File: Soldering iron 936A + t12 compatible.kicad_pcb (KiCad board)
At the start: 2 copper layers, 97 x 67 mm, 112 parts, among them J1 DC INPUT, J2 USB TO SERIAL, J3 AC input, J4 output_connector, J5 mosfet_driver_future_backup, J6 OLED, J7 USB C BREAKOUT BOARD, Q1 IRF9540N, Q2 BC547, SW1 RotaryEncoder_Switch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

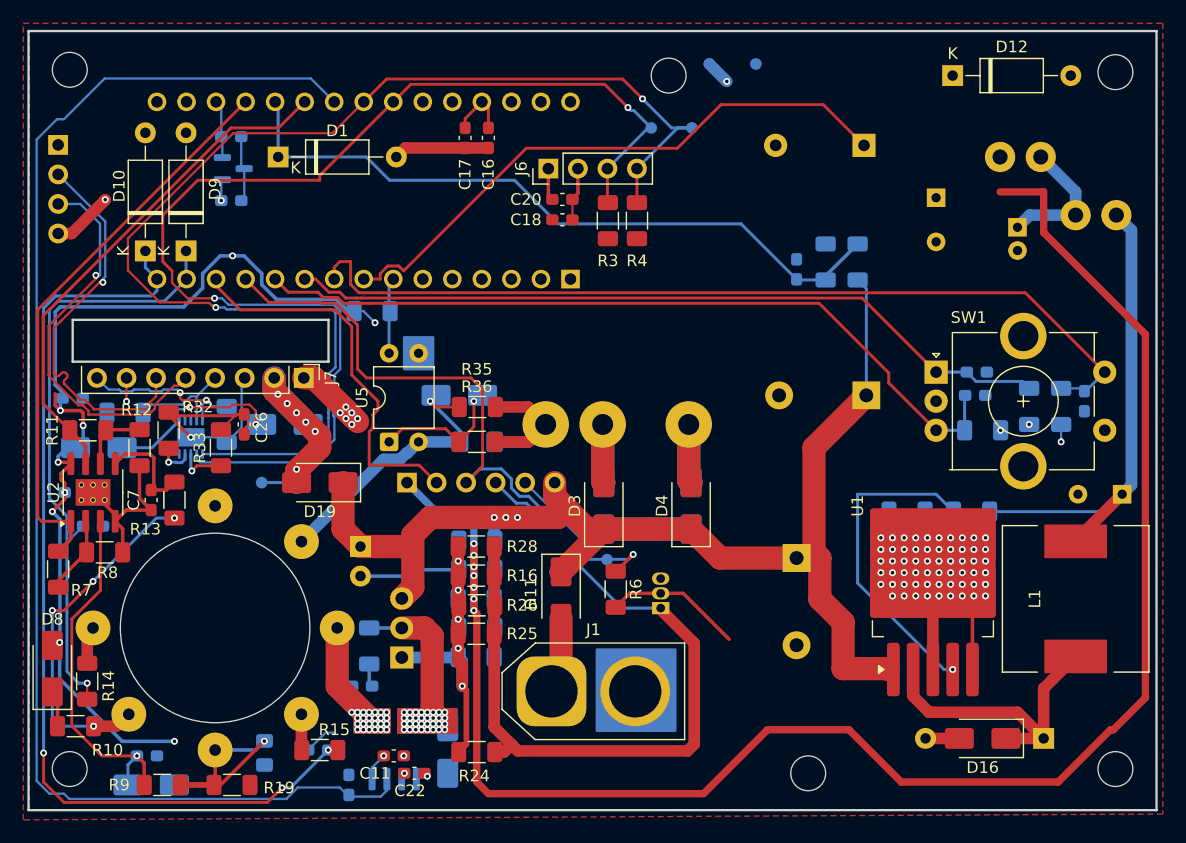
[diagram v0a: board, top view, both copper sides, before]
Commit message: added ESD diodes
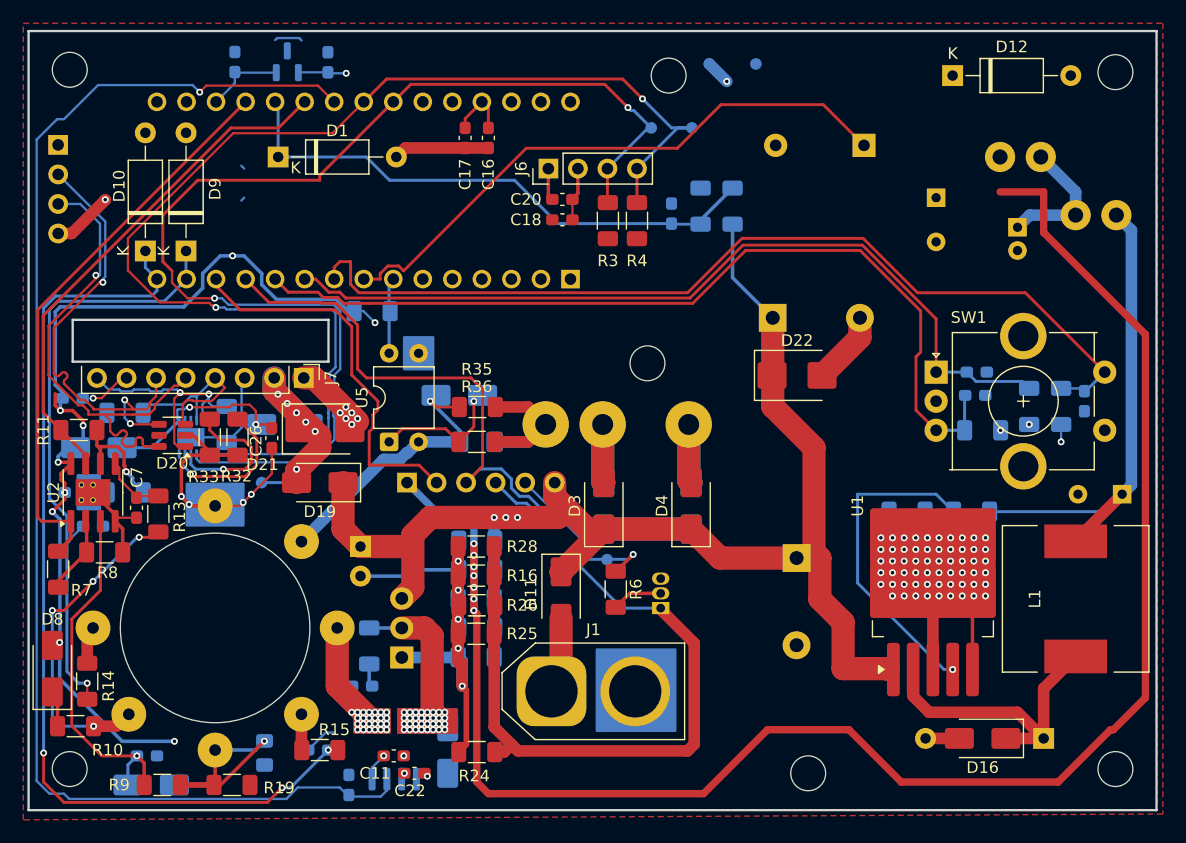
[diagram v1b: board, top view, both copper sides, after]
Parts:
- added D20: ESDA6V1-5SC6, Package_TO_SOT_SMD:SOT-23-6, F.Cu at (183.3, 100.9)
- added D21: SMBJ24A, Diode_SMD:D_SMB, F.Cu at (196.4, 100.4)
- added D22: SMBJ45A, Diode_SMD:D_SMB, F.Cu at (237.0, 95.8)
- R12: moved to B.Cu
- moved C27 14.5 mm to (196.7, 68.9), turned to 90 degrees
- moved C10 11.8 mm to (226.2, 81.9)
- moved R1 11.8 mm to (228.7, 81.2)
- moved R2 11.8 mm to (231.5, 81.2)
- moved C24 10.5 mm to (234.9, 90.8), turned to 0 degrees
- moved U6 10.3 mm to (193.2, 68.8), turned to 90 degrees
- moved C28 6.42 mm to (188.7, 68.8), turned to 90 degrees
- moved R32 5.95 mm to (188.9, 101.1), turned to -90 degrees
- moved R12 4.03 mm to (179.3, 105.8), turned to 0 degrees
- moved C26 2.64 mm to (191.9, 101.2), turned to -90 degrees
- moved R13 1.83 mm to (182.1, 107.7)
- moved C7 1.43 mm to (180.2, 107.2)
- moved R33 1.32 mm to (186.5, 101.1), turned to -90 degrees
- moved R11 0.77 mm to (175.3, 100.5)
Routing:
- net /VIN_ADC: track 60.4 -> 47.7 mm
- net Net-(U4-ISET): track 3.20 -> 13.0 mm
- net GND: track 105.7 -> 115.2 mm, vias 70 -> 73
- net /D-: track 34.2 -> 43.7 mm
- net /ENCODER B: track 68.2 -> 77.0 mm
- net Net-(U4-Vset): track 4.18 -> 13.0 mm
- net Net-(Q2-B): track 11.9 -> 4.36 mm
- net /CC1: track 9.52 -> 16.8 mm
- net /ENCODER A: track 66.2 -> 72.6 mm
- net /CC2: track 14.6 -> 21.0 mm
- net /D+: track 34.2 -> 40.0 mm, vias 1 -> 3
- net /VIN: track 117.7 -> 123.3 mm
- net /ENCODER S: track 77.3 -> 81.2 mm
- net Net-(U2B--): track 5.99 -> 9.56 mm, vias 0 -> 1
- net Net-(U2B-+): track 8.93 -> 5.43 mm
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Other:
- outline, holes or cut-outs redrawn

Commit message: added esd , oled support headers , oled switchable pinout
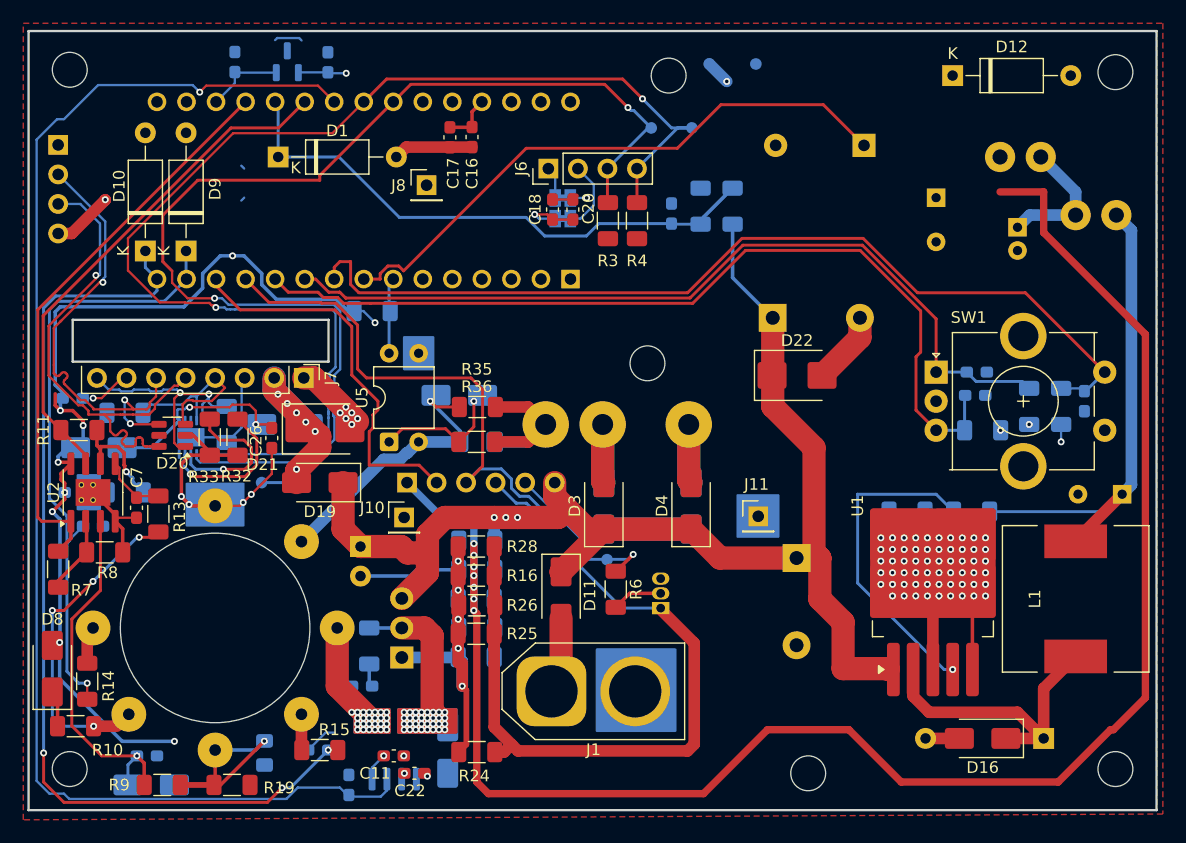
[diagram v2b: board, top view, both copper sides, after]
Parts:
- added J10: Conn_01x01_Socket, Connector_PinHeader_2.54mm:PinHeader_1x01_P2.54mm_Vertical, F.Cu at (203.3, 108.0)
- added J11: Conn_01x01_Socket, Connector_PinHeader_2.54mm:PinHeader_1x01_P2.54mm_Vertical, F.Cu at (233.7, 107.9)
- added J8: Conn_01x01_Socket, Connector_PinHeader_2.54mm:PinHeader_1x01_P2.54mm_Vertical, F.Cu at (205.2, 79.4)
- added JP1: SolderJumper_2_Bridged, Jumper:SolderJumper-2_P1.3mm_Bridged_Pad1.0x1.5mm, B.Cu at (216.9, 80.5)
- added JP2: SolderJumper_2_Bridged, Jumper:SolderJumper-2_P1.3mm_Bridged_Pad1.0x1.5mm, B.Cu at (216.9, 82.3)
- moved C16 1.41 mm to (209.1, 75.3)
- moved C17 1.31 mm to (207.2, 75.3)
- moved C20 1.26 mm to (217.8, 81.5), turned to -90 degrees
- moved C18 1.22 mm to (216.0, 81.5), turned to -90 degrees
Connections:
- J6 pad 1: +5V -> Net-(J6-SDA)
- J6 pad 2: GND -> Net-(J6-SCL)
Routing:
- net Net-(J6-SCL): track 0.00 -> 6.21 mm
- net Net-(J6-SDA): track 0.00 -> 2.77 mm
- net /VIN_ADC: track 47.7 -> 48.6 mm
- net GND: track 115.2 -> 114.6 mm, vias 73 -> 74
- net +5V: track 254.2 -> 254.1 mm, vias 22 -> 23
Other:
- board text added: "5v - 1 GND - 2"
- board text added: "5v - 2 GND - 1"
- board text added: "JP1 JP2"

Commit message: sent for FAB , case also designed, lets hope for best
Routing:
- net /VIN: track 123.6 -> 122.9 mm
- net Net-(D17-K): track 17.2 -> 16.6 mm
- net /P+: vias 25 -> 12
- net /MOS_OUT: vias 32 -> 18

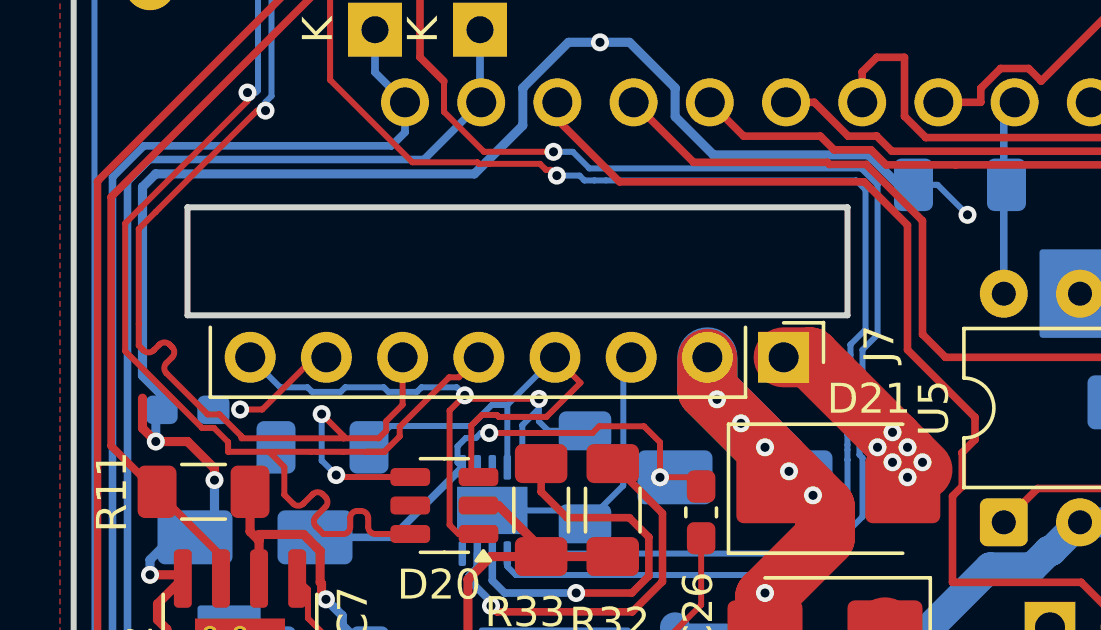
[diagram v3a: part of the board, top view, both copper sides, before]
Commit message: Added castellated edges
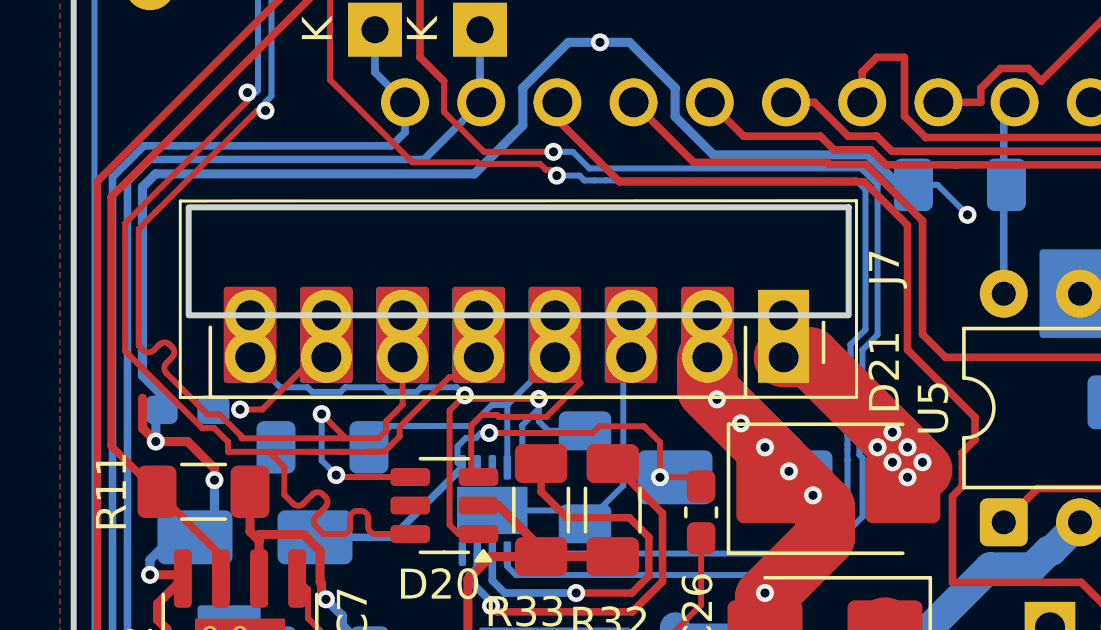
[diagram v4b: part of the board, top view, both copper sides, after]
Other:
- outline, holes or cut-outs redrawn

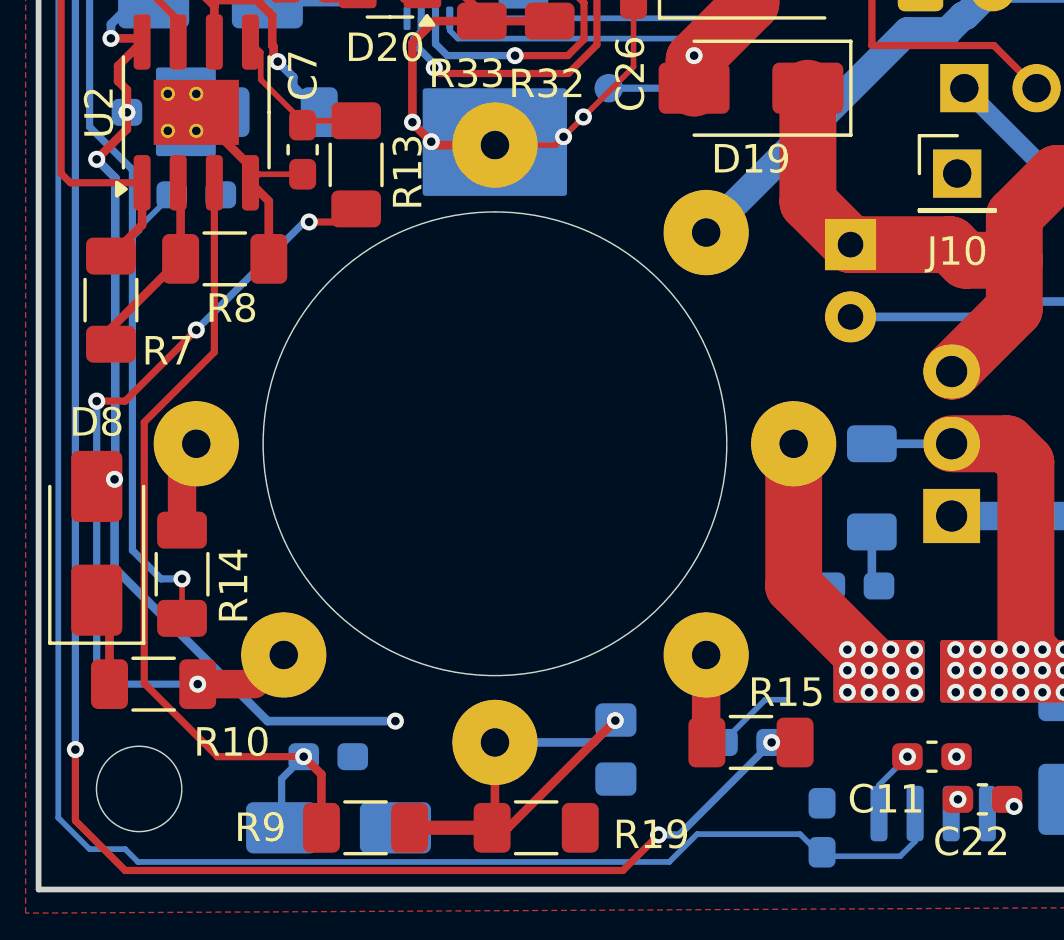
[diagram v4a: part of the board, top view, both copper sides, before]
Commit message: updated foot print of gx 16 connector
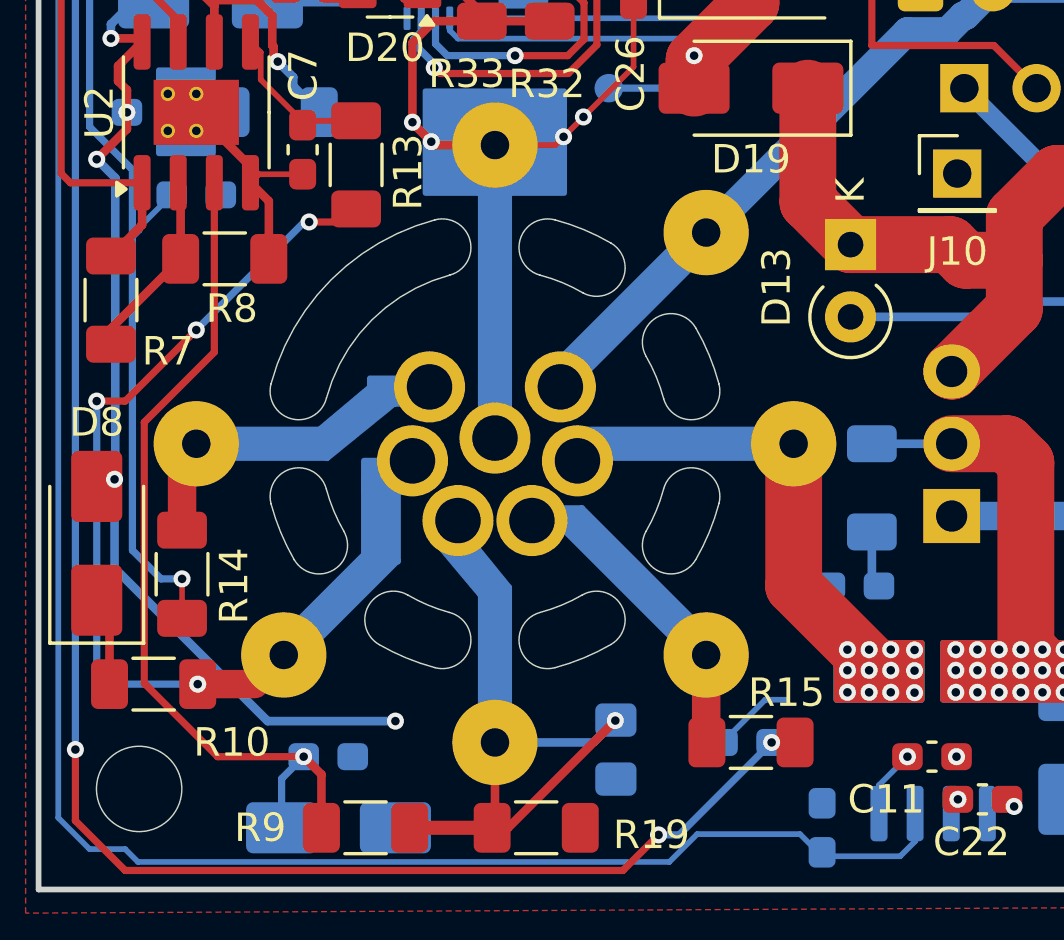
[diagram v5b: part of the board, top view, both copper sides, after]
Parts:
- D13: moved to F.Cu
